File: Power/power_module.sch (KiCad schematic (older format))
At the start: 51 parts, among them J1 Conn_02x03_Odd_Even, J2 Conn_02x03_Odd_Even, J3 Conn_02x06_Counter_Clockwise, J4 Conn_02x05_Top_Bottom, J5 Conn_02x05_Top_Bottom, J6 Conn_02x02_Odd_Even, J7 Conn_02x02_Odd_Even, P3 CONN_01X04, P6 CONN_01X04, Q1 Q_NMOS_GDS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

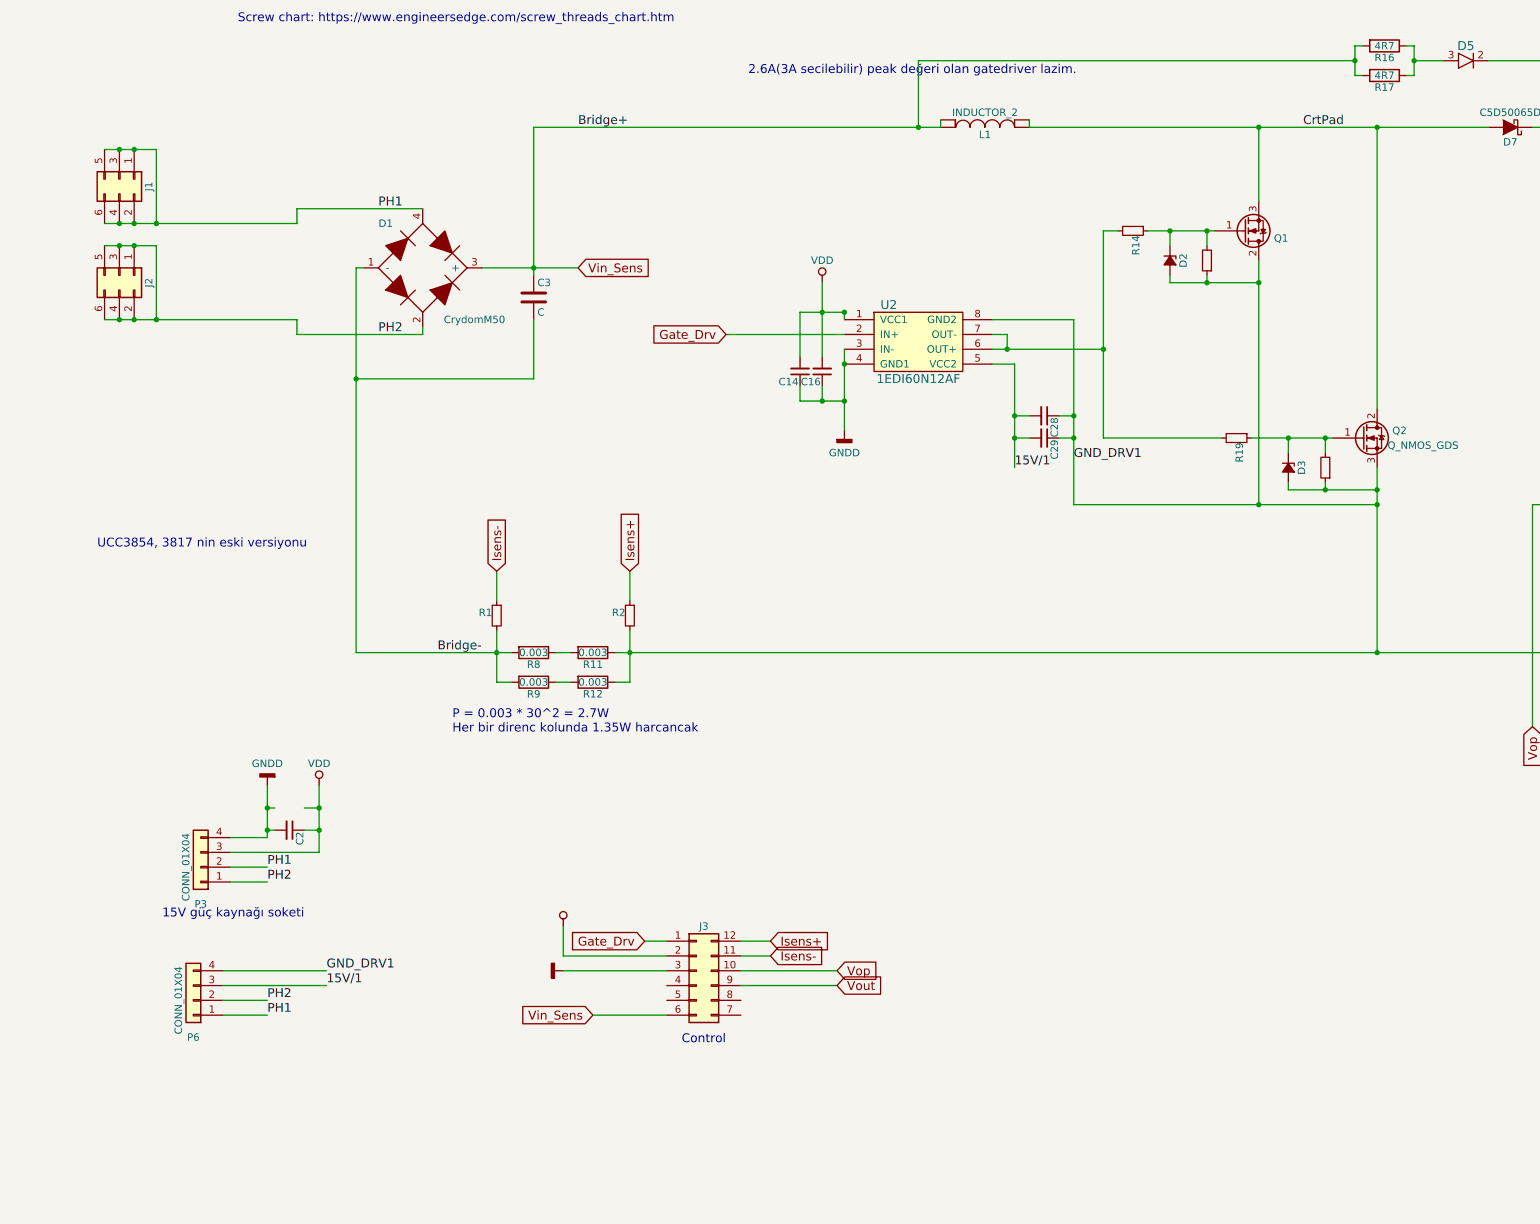
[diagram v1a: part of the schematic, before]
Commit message: Guc akisindaki hat/poligonlar tamamlandi.
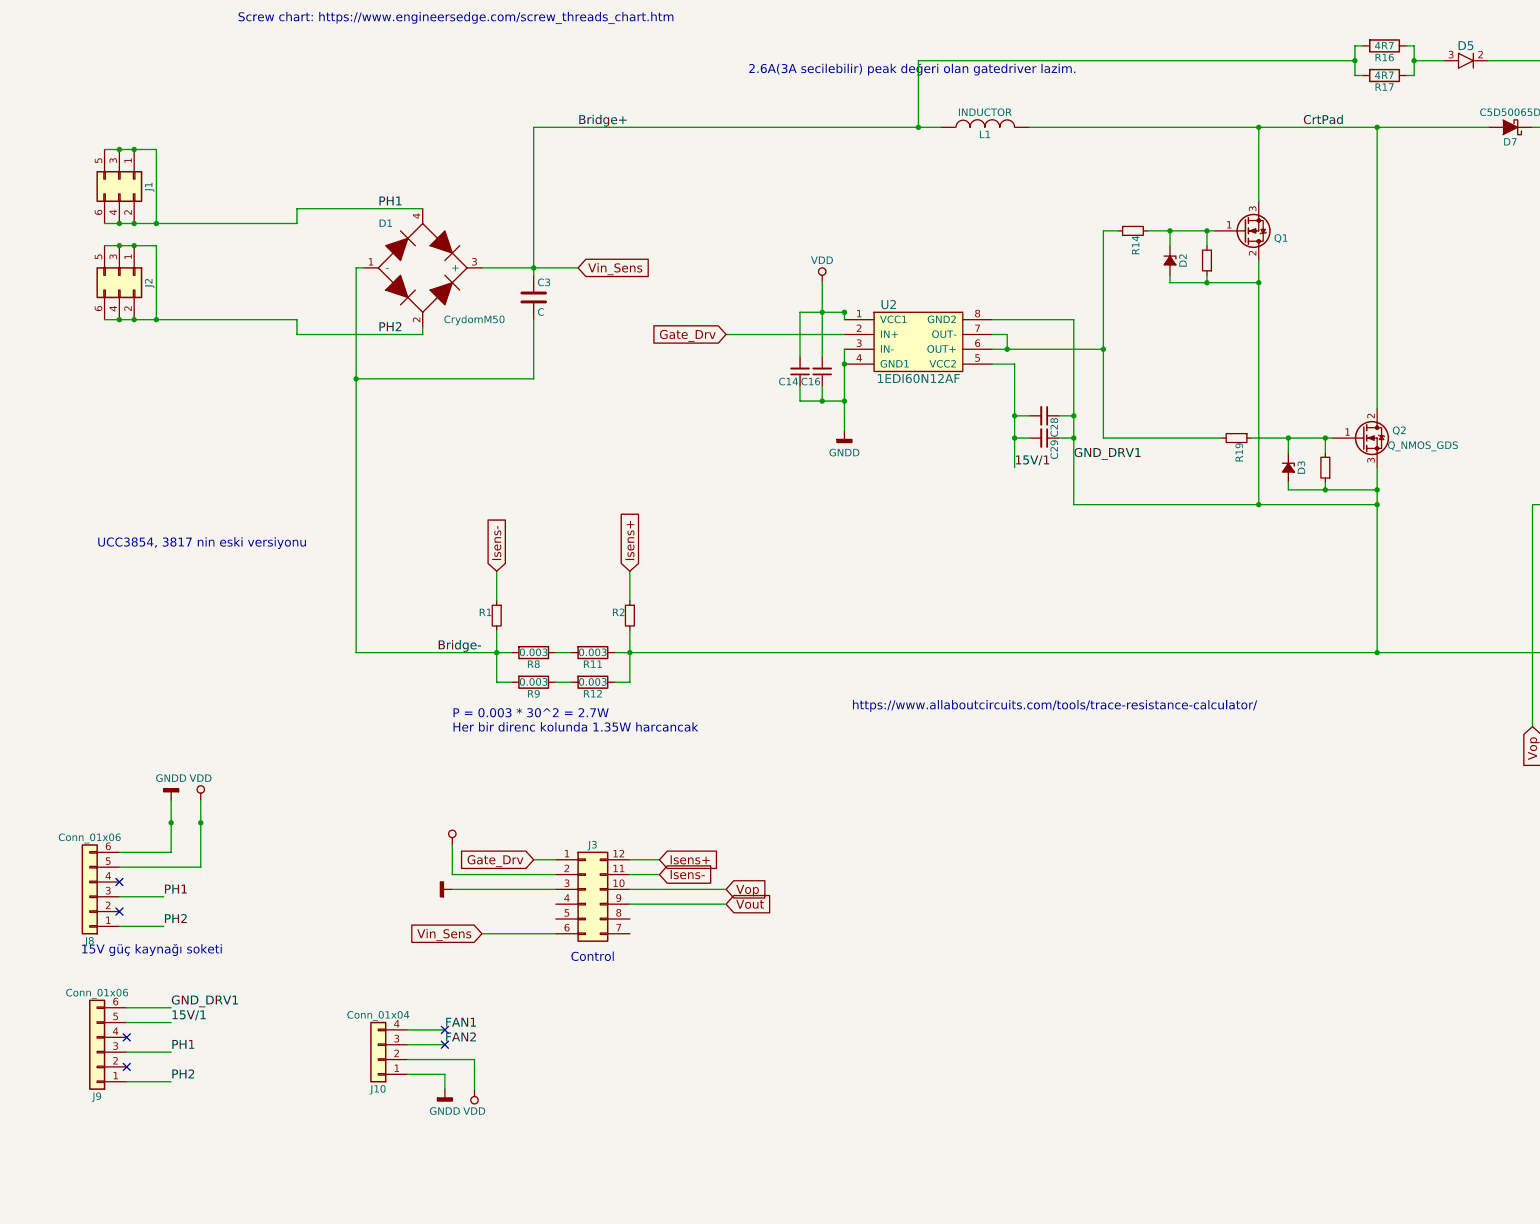
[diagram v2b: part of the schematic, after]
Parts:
- removed C2: 100n, Capacitors_SMD:C_0805_HandSoldering, symbol C_Small
- removed L1: INDUCTOR_2, NamchoLibs:OD_77.80xID_39.34xHT_25.85_Vertical, symbol INDUCTOR_2
- removed P3, P6: CONN_01X04, Pin_Headers:Pin_Header_Straight_1x04_Pitch2.54mm, symbol Conn_01x04
- added J10: Conn_01x04, Pin_Headers:Pin_Header_Straight_1x04_Pitch2.54mm, symbol Conn_01x04
- added J8, J9: Conn_01x06, Pin_Headers:Pin_Header_Straight_1x06_Pitch2.54mm, symbol Conn_01x06
- added L1: INDUCTOR, NamchoLibs:OD_77.80xID_39.34xHT_25.85_Vertical, symbol INDUCTOR
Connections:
- net 15V/1: now also J9.5 (Pin_5)
- net CrtPad: now also L1.1
- net GNDA: now also J9.6 (Pin_6)
- net GNDD: now also J10.1 (Pin_1), J8.6 (Pin_6)
- net PH1: now also J8.3 (Pin_3), J9.3 (Pin_3)
- net PH2: now also J8.1 (Pin_1), J9.1 (Pin_1)
- net VDD: now also J10.2 (Pin_2), J8.5 (Pin_5)
- net Vin_Sens: now also L1.2
- new net FAN1: J10.4 (Pin_4)
- new net FAN2: J10.3 (Pin_3)
- no-connect marks 6 -> 12
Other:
- note added: "https://www.allaboutcircuits.com/tools/trace-resistance-calculator/"
- moved on the sheet: J3
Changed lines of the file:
@@
-$EndComp
-$Comp
-L Conn_01x04 P3
-U 1 1 5A611909
-P 1650 7000
-F 0 "P3" H 1650 7250 50  0000 C CNN
-F 1 "CONN_01X04" V 1750 7000 50  0000 C CNN
-F 2 "Pin_Headers:Pin_Header_Straight_1x04_Pitch2.54mm" H 1650 7000 50  0001 C CNN
-F 3 "" H 1650 7000 50  0000 C CNN
-	1    1650 7000
-	-1   0    0    1
 $EndComp
 $Comp
 L GNDD #PWR04
 U 1 1 5A6130FA
-P 2100 6450
-F 0 "#PWR04" H 2100 6200 50  0001 C CNN
-F 1 "GNDD" H 2100 6300 50  0000 C CNN
-F 2 "" H 2100 6450 50  0000 C CNN
-F 3 "" H 2100 6450 50  0000 C CNN
-	1    2100 6450
+P 1450 6550
+F 0 "#PWR04" H 1450 6300 50  0001 C CNN
+F 1 "GNDD" H 1450 6400 50  0000 C CNN
+F 2 "" H 1450 6550 50  0000 C CNN
+F 3 "" H 1450 6550 50  0000 C CNN
+	1    1450 6550
 	-1   0    0    1
 $EndComp
-Text Notes 2350 7350 2    60   ~ 0
+Text Notes 1800 7600 2    60   ~ 0
 15V güç kaynağı soketi
 Text Label 2850 2550 0    60   ~ 0
@@
 Text Label 2850 3400 0    60   ~ 0
 PH2
-Text Label 2100 7100 0    60   ~ 0
-PH2
-Text Label 2100 7000 0    60   ~ 0
-PH1
-$Comp
-L C_Small C2
-U 1 1 5A61672E
-P 2250 6750
-F 0 "C2" H 2260 6820 50  0000 L CNN
-F 1 "100n" H 2260 6670 50  0001 L CNN
-F 2 "Capacitors_SMD:C_0805_HandSoldering" H 2250 6750 50  0001 C CNN
-F 3 "" H 2250 6750 50  0000 C CNN
-	1    2250 6750
-	0    1    1    0
-$EndComp
 $Comp
 L Q_NMOS_GDS Q2
@@
 Connection ~ 12050 2000
 Wire Wire Line
-	2450 6750 2350 6750
-Wire Wire Line
-	2100 6800 1850 6800
-Wire Wire Line
-	2450 6900 1850 6900
-Wire Wire Line
-	1850 7000 2100 7000
-Wire Wire Line
-	1850 7100 2100 7100
-Wire Wire Line
 	13950 5550 13950 4200
 Wire Wire Line
@@
 NoConn ~ 15300 7750
 NoConn ~ 14350 7750
-$Comp
-L Conn_01x04 P6
-U 1 1 5A9611CB
-P 1600 7900
-F 0 "P6" H 1600 8150 50  0000 C CNN
-F 1 "CONN_01X04" V 1700 7900 50  0000 C CNN
-F 2 "Pin_Headers:Pin_Header_Straight_1x04_Pitch2.54mm" H 1600 7900 50  0001 C CNN
-F 3 "" H 1600 7900 50  0000 C CNN
-	1    1600 7900
-	-1   0    0    1
-$EndComp
-$Comp
-L INDUCTOR_2 L1
-U 1 1 5A962438
-P 6950 2000
-F 0 "L1" V 6900 2000 50  0000 C CNN
-F 1 "INDUCTOR_2" V 7050 2000 50  0000 C CNN
-F 2 "NamchoLibs:OD_77.80xID_39.34xHT_25.85_Vertical" H 6950 2000 50  0001 C CNN
-F 3 "" H 6950 2000 50  0000 C CNN
-	1    6950 2000
-	0    -1   -1   0
-$EndComp
 Text Label 13950 2000 0    60   ~ 0
 Vout+
@@
 Text Label 7550 4250 0    60   ~ 0
 GND_DRV1
-Wire Wire Line
-	1800 8000 2100 8000
-Wire Wire Line
-	1800 7900 2100 7900
-Wire Wire Line
-	1800 7800 2500 7800
-Wire Wire Line
-	1800 7700 2500 7700
-Text Label 2100 7900 0    60   ~ 0
-PH2
-Text Label 2100 8000 0    60   ~ 0
-PH1
 Wire Wire Line
 	7150 3600 7150 4300
@@
 15V/1
 Connection ~ 6000 3600
-Text Label 2500 7800 0    60   ~ 0
-15V/1
-Wire Wire Line
-	2450 6450 2450 6900
-Wire Wire Line
-	2350 6600 2450 6600
-Connection ~ 2450 6600
-Wire Wire Line
-	2100 6450 2100 6800
-Wire Wire Line
-	2100 6750 2150 6750
-Connection ~ 2100 6750
-Wire Wire Line
-	2100 6600 2150 6600
-Connection ~ 2100 6600
-Connection ~ 2450 6750
 $Comp
 L Q_NMOS_GDS Q1
@@
 Connection ~ 8800 4550
 Connection ~ 8800 2000
-Wire Wire Line
-	6650 2000 6650 1950
-Wire Wire Line
-	7250 1950 7250 2000
 Wire Wire Line
 	6500 1550 6500 2000
@@
 L Conn_02x06_Counter_Clockwise J3
 U 1 1 5AF80F5B
-P 5000 7700
-F 0 "J3" H 5050 8000 50  0000 C CNN
-F 1 "Conn_02x06_Counter_Clockwise" H 5050 7300 50  0001 C CNN
-F 2 "NamchoLibs:Harwin_M55_6001242R" H 5000 7700 50  0001 C CNN
-F 3 "https://www.mouser.com.tr/datasheet/2/181/M55-60X-1286666.pdf" H 5000 7700 50  0001 C CNN
-	1    5000 7700
-	1    0    0    -1
-$EndComp
-Text Notes 4900 8200 0    60   ~ 0
+P 4250 7150
+F 0 "J3" H 4300 7450 50  0000 C CNN
+F 1 "Conn_02x06_Counter_Clockwise" H 4300 6750 50  0001 C CNN
+F 2 "NamchoLibs:Harwin_M55_6001242R" H 4250 7150 50  0001 C CNN
+F 3 "https://www.mouser.com.tr/datasheet/2/181/M55-60X-1286666.pdf" H 4250 7150 50  0001 C CNN
+	1    4250 7150
+	1    0    0    -1
+$EndComp
+Text Notes 4150 7650 0    60   ~ 0
 Control
-Text Label 2500 7700 0    60   ~ 0
-GND_DRV1
 $Comp
 L VDD #PWR06
 U 1 1 5AFA1D8A
-P 2450 6450
-F 0 "#PWR06" H 2450 6300 50  0001 C CNN
-F 1 "VDD" H 2450 6600 50  0000 C CNN
-F 2 "" H 2450 6450 50  0001 C CNN
-F 3 "" H 2450 6450 50  0001 C CNN
-	1    2450 6450
+P 1650 6550
+F 0 "#PWR06" H 1650 6400 50  0001 C CNN
+F 1 "VDD" H 1650 6700 50  0000 C CNN
+F 2 "" H 1650 6550 50  0001 C CNN
+F 3 "" H 1650 6550 50  0001 C CNN
+	1    1650 6550
 	1    0    0    -1
 $EndComp
@@
 L VDD #PWR08
 U 1 1 5AFA6CCC
-P 4100 7400
-F 0 "#PWR08" H 4100 7250 50  0001 C CNN
-F 1 "VDD" H 4100 7550 50  0001 C CNN
-F 2 "" H 4100 7400 50  0001 C CNN
-F 3 "" H 4100 7400 50  0001 C CNN
-	1    4100 7400
+P 3350 6850
+F 0 "#PWR08" H 3350 6700 50  0001 C CNN
+F 1 "VDD" H 3350 7000 50  0001 C CNN
+F 2 "" H 3350 6850 50  0001 C CNN
+F 3 "" H 3350 6850 50  0001 C CNN
+	1    3350 6850
 	1    0    0    -1
 $EndComp
@@
 L GNDD #PWR09
 U 1 1 5AFA737B
-P 4100 7700
-F 0 "#PWR09" H 4100 7450 50  0001 C CNN
-F 1 "GNDD" H 4100 7550 50  0001 C CNN
-F 2 "" H 4100 7700 50  0000 C CNN
-F 3 "" H 4100 7700 50  0000 C CNN
-	1    4100 7700
+P 3350 7150
+F 0 "#PWR09" H 3350 6900 50  0001 C CNN
+F 1 "GNDD" H 3350 7000 50  0001 C CNN
+F 2 "" H 3350 7150 50  0000 C CNN
+F 3 "" H 3350 7150 50  0000 C CNN
+	1    3350 7150
 	0    1    -1   0
 $EndComp
-Text GLabel 4650 7500 0    60   Input ~ 0
+Text GLabel 3900 6950 0    60   Input ~ 0
 Gate_Drv
-Text GLabel 5500 7500 2    60   Input ~ 0
+Text GLabel 4750 6950 2    60   Input ~ 0
 Isens+
-Text GLabel 5500 7600 2    60   Input ~ 0
+Text GLabel 4750 7050 2    60   Input ~ 0
 Isens-
 Wire Wire Line
-	5500 7500 5300 7500
-Wire Wire Line
-	5500 7600 5300 7600
-Text GLabel 5950 7700 2    60   Input ~ 0
+	4750 6950 4550 6950
+Wire Wire Line
+	4750 7050 4550 7050
+Text GLabel 5200 7150 2    60   Input ~ 0
 Vop
-Text GLabel 5950 7800 2    60   Input ~ 0
+Text GLabel 5200 7250 2    60   Input ~ 0
 Vout
 Wire Wire Line
-	5950 7700 5300 7700
-Wire Wire Line
-	5300 7800 5950 7800
-Text GLabel 4300 8000 0    60   Input ~ 0
+	5200 7150 4550 7150
+Wire Wire Line
+	4550 7250 5200 7250
+Text GLabel 3550 7450 0    60   Input ~ 0
 Vin_Sens
 Wire Wire Line
-	4800 8000 4300 8000
-Wire Wire Line
-	9600 4300 9600 5550
+	4050 7450 3550 7450
+Wire Wire Line
+	9600 5550 9600 4300
 Wire Wire Line
 	13950 3350 14450 3350
@@
 	4550 5000 4550 5200
 Wire Wire Line
-	4650 7500 4800 7500
-Wire Wire Line
-	4100 7400 4100 7600
-Wire Wire Line
-	4100 7600 4800 7600
-Wire Wire Line
-	4100 7700 4800 7700
+	3900 6950 4050 6950
+Wire Wire Line
+	3350 6850 3350 7050
+Wire Wire Line
+	3350 7050 4050 7050
+Wire Wire Line
+	3350 7150 4050 7150
 Wire Wire Line
 	10350 1550 13050 1550
+$Comp
+L INDUCTOR L1
+U 1 1 5AFAD4CB
+P 6950 2000
+F 0 "L1" V 6900 2000 50  0000 C CNN
+F 1 "INDUCTOR" V 7050 2000 50  0000 C CNN
+F 2 "NamchoLibs:OD_77.80xID_39.34xHT_25.85_Vertical" H 6950 2000 50  0001 C CNN
+F 3 "" H 6950 2000 50  0000 C CNN
+	1    6950 2000
+	0    -1   -1   0
+$EndComp
+$Comp
+L Conn_01x06 J9
+U 1 1 5AFB3838
+P 950 8250
+F 0 "J9" H 950 8550 50  0000 C CNN
+F 1 "Conn_01x06" H 950 7850 50  0000 C CNN
+F 2 "Pin_Headers:Pin_Header_Straight_1x06_Pitch2.54mm" H 950 8250 50  0001 C CNN
+F 3 "" H 950 8250 50  0001 C CNN
+	1    950  8250
+	-1   0    0    1
+$EndComp
+Wire Wire Line
+	1150 8450 1450 8450
+Wire Wire Line
+	1150 8250 1450 8250
+Wire Wire Line
+	1150 8050 1450 8050
+Wire Wire Line
+	1150 7950 1450 7950
+Text Label 1450 8250 0    60   ~ 0
+PH1
+Text Label 1450 8450 0    60   ~ 0
+PH2
+Text Label 1450 8050 0    60   ~ 0
+15V/1
+Text Label 1450 7950 0    60   ~ 0
+GND_DRV1
+$Comp
+L Conn_01x06 J8
+U 1 1 5AFB640A
+P 900 7200
+F 0 "J8" H 900 7500 50  0000 C CNN
+F 1 "Conn_01x06" H 900 6800 50  0000 C CNN
+F 2 "Pin_Headers:Pin_Header_Straight_1x06_Pitch2.54mm" H 900 7200 50  0001 C CNN
+F 3 "" H 900 7200 50  0001 C CNN
+	1    900  7200
+	-1   0    0    1
+$EndComp
+Wire Wire Line
+	1100 7400 1400 7400
+Wire Wire Line
+	1100 7200 1400 7200
+Text Label 1400 7400 0    60   ~ 0
+PH2
+Text Label 1400 7200 0    60   ~ 0
+PH1
+Wire Wire Line
+	1450 6900 1100 6900
+Wire Wire Line
+	1450 6550 1450 6900
+Connection ~ 1450 6700
+Wire Wire Line
+	1650 6550 1650 7000
+Wire Wire Line
+	1650 7000 1100 7000
+Connection ~ 1650 6700
+$Comp
+L Conn_01x04 J10
+U 1 1 5AFBB4A6
+P 2850 8300
+F 0 "J10" H 2850 8500 50  0000 C CNN
+F 1 "Conn_01x04" H 2850 8000 50  0000 C CNN
+F 2 "Pin_Headers:Pin_Header_Straight_1x04_Pitch2.54mm" H 2850 8300 50  0001 C CNN
+F 3 "" H 2850 8300 50  0001 C CNN
+	1    2850 8300
+	-1   0    0    1
+$EndComp
+Wire Wire Line
+	3050 8400 3300 8400
+Wire Wire Line
+	3050 8300 3500 8300
+Wire Wire Line
+	3050 8200 3300 8200
+Wire Wire Line
+	3050 8100 3300 8100
+$Comp
+L GNDD #PWR010
+U 1 1 5AFBE4B4
+P 3300 8500
+F 0 "#PWR010" H 3300 8250 50  0001 C CNN
+F 1 "GNDD" H 3300 8350 50  0000 C CNN
+F 2 "" H 3300 8500 50  0000 C CNN
+F 3 "" H 3300 8500 50  0000 C CNN
+	1    3300 8500
+	1    0    0    -1
+$EndComp
+Wire Wire Line
+	3300 8400 3300 8500
+$Comp
+L VDD #PWR011
+U 1 1 5AFBF9F8
+P 3500 8500
+F 0 "#PWR011" H 3500 8350 50  0001 C CNN
+F 1 "VDD" H 3500 8650 50  0000 C CNN
+F 2 "" H 3500 8500 50  0001 C CNN
+F 3 "" H 3500 8500 50  0001 C CNN
+	1    3500 8500
+	-1   0    0    1
+$EndComp
+Wire Wire Line
+	3500 8300 3500 8500
+Text Label 3300 8100 0    60   ~ 0
+FAN1
+Text Label 3300 8200 0    60   ~ 0
+FAN2
+NoConn ~ 3300 8100
+NoConn ~ 3300 8200
+NoConn ~ 1150 8350
+NoConn ~ 1150 8150
+NoConn ~ 1100 7300
+NoConn ~ 1100 7100
+Text Notes 6050 5950 0    60   ~ 0
+https://www.allaboutcircuits.com/tools/trace-resistance-calculator/
 $EndSCHEMATC

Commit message: Poligon eklemeleri yapildi. Hatlar iyilestirildi.
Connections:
- net Gate1: now reaches D2.1 (K), Q1.1 (G), R14.1, R31.2
- net Drv_Out: now reaches R14.2, R19.2, U2.6 (OUT+), U2.7 (OUT-)
- net Gate2: now reaches D3.1 (K), Q2.1 (G), R19.1, R32.2
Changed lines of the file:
@@
 Text Notes 6050 5950 0    60   ~ 0
 https://www.allaboutcircuits.com/tools/trace-resistance-calculator/
+Text Label 8200 2700 0    60   ~ 0
+Gate1
+Text Label 9000 4100 0    60   ~ 0
+Gate2
+Text Label 7750 3500 0    60   ~ 0
+Drv_Out
 $EndSCHEMATC

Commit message: Güc kartina EMI filtresi eklendi. Güc kartindaki mosfet driver + ve - ile beslenebilecek sekilde duzenlendi. Güc ve kontrol kartlari icin BOM uretildi.
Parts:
- removed C29: 10n, Capacitors_SMD:C_0805_HandSoldering, symbol C_Small
- removed R15: R_Small, Resistors_SMD:R_0805_HandSoldering, symbol R_Small
- added C1: 1u, Capacitors_SMD:C_1206_HandSoldering, symbol C_Small
- added C2, C4: C, Capacitors_ThroughHole:CP_Axial_L30.0mm_D10.0mm_P35.00mm_Horizontal, symbol C
- added C5, C6: 100n, Capacitors_ThroughHole:C_Rect_L18.0mm_W8.0mm_P15.00mm_FKS3_FKP3, symbol C
- added FL1: EMI_Filter_CommonMode, NamchoLibs:RB6522_Size4, symbol EMI_Filter_CommonMode
- added J11: Conn_02x02_Odd_Even, NamchoLibs:Conn_4pins_15A, symbol Conn_02x02_Odd_Even
- added R3: R_Small, Resistors_SMD:R_0805_HandSoldering, symbol R_Small
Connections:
- net GNDD is gone; now on net GNDA: C14.1, C16.1, J10.1 (Pin_1), J3.3 (Pin_3), J8.6 (Pin_6), U2.3 (IN-), U2.4 (GND1)
- net 15V/1: now also C28.1; no longer C28.2
- net GNDA: now also C28.2, C1.2, R3.2; no longer C28.1, J9.6 (Pin_6), U2.8 (GND2)
- net PH1: now also D1.2, J8.1 (Pin_1), J9.1 (Pin_1), C4.1, C5.2, FL1.2; no longer D1.4, J1.1 (Pin_1), J1.2 (Pin_2), J1.3 (Pin_3), J1.4 (Pin_4), J1.5 (Pin_5), J1.6 (Pin_6), J8.3 (Pin_3), J9.3 (Pin_3)
- net PH2: now also D1.4, J8.3 (Pin_3), J9.3 (Pin_3), C4.2, C6.1, FL1.4; no longer D1.2, J2.1 (Pin_1), J2.2 (Pin_2), J2.3 (Pin_3), J2.4 (Pin_4), J2.5 (Pin_5), J2.6 (Pin_6), J8.1 (Pin_1), J9.1 (Pin_1)
- net Earth: now reaches MP6.1
- net Earth: now also C5.1, C6.2, J11.1 (Pin_1), J11.2 (Pin_2), J11.3 (Pin_3), J11.4 (Pin_4)
- new net GND_DRV1: C1.1, J9.6 (Pin_6), R3.1, U2.8 (GND2)
- new net Line1: C2.1, FL1.1, J2.1 (Pin_1), J2.2 (Pin_2), J2.3 (Pin_3), J2.4 (Pin_4), J2.5 (Pin_5), J2.6 (Pin_6)
- new net Line2: C2.2, FL1.3, J1.1 (Pin_1), J1.2 (Pin_2), J1.3 (Pin_3), J1.4 (Pin_4), J1.5 (Pin_5), J1.6 (Pin_6)
- no-connect marks 12 -> 11
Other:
- note removed: "Cikis kondasatorleri Panasonic 450V 390uF 30mmx45mm secildi."
- moved on the sheet: C14, C16, C28, J1, J2, MP6, U2
